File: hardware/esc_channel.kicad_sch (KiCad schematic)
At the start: 17 parts, among them Q32 AGM210MAP, Q33 AGM210MAP, Q34 AGM210MAP, U7 EFM8BB51F16I

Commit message: WIP hand-off: board sync progress, schematic readability edits (esc/pads/rx sheets), PDF; not yet verified
Co-Authored-By: Claude Opus 5.5 <noreply@anthropic.com>
Claude-Session: https://claude.ai/code/session_01RFaS5jnC9tnPam9GBgmGnG
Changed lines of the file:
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@@
 	(text_box "Power-up: the EFM8 runs from the cell before the FC's 3.3 V is up; its weak pull-up can put <= 60 uA on the FC DShot pad (0.72 V over the unpowered-FT limit, current-limited). Accepted on Matrix parity; V9 scopes it.\nUSB only: DShot idle-high back-feeds +BATT through the EFM8 I/O diode (about 1 mA per channel)."
 		(exclude_from_sim no)
-		(at 203.2 96.52 0)
+		(at 203.2 41.91 0)
 		(size 81.28 15.24)
 		(margins 0.9525 0.9525 0.9525 0.9525)

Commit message: Trim BOM to strictly needed parts, fill sourcing fields, fix library datasheets
Owner review 2026-10-11, schematic only (board not resynced).

Removed (17 parts): D1 TVS (clamps above every IC abs max), R2/R3/C5
INA186 input RC, U5 TPS22810 O4 switch with C16/C129/R9/R10/R87/D2
(VHD pad now on +5V_BST, as Matrix HD boards; HD_EN still holds the
analog VTX off via Q28, R11 kept), R67 selector (PA_VCC is +BATT),
TH1/R70 PA NTC and R84 (patched-ELRS only; GPIO37/GPIO4 no-connect),
C92 and C121 (beyond SX1281 / LP5912 datasheet decoupling).

Changed: D4 WS2812 VDD to +5V (3.5 V min); X3 TCXO pin 1 floating per
the YXC sheet; C122/C123/C134 4.7 uF 0402 -> 0201 GRM035R60J475ME15D.

Sourcing: LCSC numbers for 21 MPN lines (SKUBAAE010 has no listing);
every BOM part keeps MPN + Manufacturer for NextPCB.

Library: 16 unused lib symbols pruned; dead or HTML-only datasheet
links replaced with verified PDF URLs (RTC6705, SE5004L, FL2, X1,
EFM8BB51, BC857BM, FTC252012, HCS1206 shunt, Molex 53047).

Net-class patterns and contract entries for the removed nets dropped;
PINMAP ESP32 rows updated (GPIO36 is ADC1_CH0).

Validation: ERC 0 errors / 2 warnings (baseline); check_netlist 7 ok;
sch_integrate --check idempotent; check_conventions unchanged.

Co-Authored-By: Claude Opus 5.5 <noreply@anthropic.com>
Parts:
- R23, R24, R25: LCSC (none) -> C138165
- U7: LCSC (none) -> C3232998
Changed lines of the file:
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@@
 		(in_pos_files no)
 		(dnp no)
-		(property "Reference" "#PWR69"
+		(property "Reference" "#PWR60"
 			(at 109.22 153.67 0)
 			(hide yes)
@@
 			(project "OpenAIO-Whoop"
 				(path "/2c3a7206-1e66-4d43-a02f-491225e20dd6/0021bee0-9959-5c9e-86f0-21e49fa9ce8d"
-					(reference "#PWR69")
+					(reference "#PWR60")
 					(unit 1)
 				)
 				(path "/2c3a7206-1e66-4d43-a02f-491225e20dd6/6d139bfe-ad39-5d26-964c-e430887c2538"
-					(reference "#PWR89")
+					(reference "#PWR80")
 					(unit 1)
 				)
 				(path "/2c3a7206-1e66-4d43-a02f-491225e20dd6/a3c0517e-76c5-5fd7-8d0f-d7e948ad3995"
-					(reference "#PWR79")
+					(reference "#PWR70")
 					(unit 1)
 				)
 				(path "/2c3a7206-1e66-4d43-a02f-491225e20dd6/d67c44eb-67d1-5da8-b7a8-40b16f9433cd"
-					(reference "#PWR59")
+					(reference "#PWR50")
 					(unit 1)
 				)
@@
 			)
 		)
-		(property "LCSC" ""
+		(property "LCSC" "C3232998"
 			(at 76.2 60.96 0)
 			(hide yes)
@@
 		(in_pos_files no)
 		(dnp no)
-		(property "Reference" "#PWR72"
+		(property "Reference" "#PWR63"
 			(at 99.06 177.8 0)
 			(hide yes)
@@
 			(project "OpenAIO-Whoop"
 				(path "/2c3a7206-1e66-4d43-a02f-491225e20dd6/0021bee0-9959-5c9e-86f0-21e49fa9ce8d"
-					(reference "#PWR72")
+					(reference "#PWR63")
 					(unit 1)
 				)
 				(path "/2c3a7206-1e66-4d43-a02f-491225e20dd6/6d139bfe-ad39-5d26-964c-e430887c2538"
-					(reference "#PWR92")
+					(reference "#PWR83")
 					(unit 1)
 				)
 				(path "/2c3a7206-1e66-4d43-a02f-491225e20dd6/a3c0517e-76c5-5fd7-8d0f-d7e948ad3995"
-					(reference "#PWR82")
+					(reference "#PWR73")
 					(unit 1)
 				)
 				(path "/2c3a7206-1e66-4d43-a02f-491225e20dd6/d67c44eb-67d1-5da8-b7a8-40b16f9433cd"
-					(reference "#PWR62")
+					(reference "#PWR53")
 					(unit 1)
 				)
@@
 			)
 		)
-		(property "LCSC" ""
+		(property "LCSC" "C138165"
 			(at 156.21 35.56 0)
 			(hide yes)
@@
 		(in_pos_files no)
 		(dnp no)
-		(property "Reference" "#PWR73"
+		(property "Reference" "#PWR64"
 			(at 142.24 177.8 0)
 			(hide yes)
@@
 			(project "OpenAIO-Whoop"
 				(path "/2c3a7206-1e66-4d43-a02f-491225e20dd6/0021bee0-9959-5c9e-86f0-21e49fa9ce8d"
-					(reference "#PWR73")
+					(reference "#PWR64")
 					(unit 1)
 				)
 				(path "/2c3a7206-1e66-4d43-a02f-491225e20dd6/6d139bfe-ad39-5d26-964c-e430887c2538"
-					(reference "#PWR93")
+					(reference "#PWR84")
 					(unit 1)
 				)
 				(path "/2c3a7206-1e66-4d43-a02f-491225e20dd6/a3c0517e-76c5-5fd7-8d0f-d7e948ad3995"
-					(reference "#PWR83")
+					(reference "#PWR74")
 					(unit 1)
 				)
 				(path "/2c3a7206-1e66-4d43-a02f-491225e20dd6/d67c44eb-67d1-5da8-b7a8-40b16f9433cd"
-					(reference "#PWR63")
+					(reference "#PWR54")
 					(unit 1)
 				)
@@
 		(in_pos_files no)
 		(dnp no)
-		(property "Reference" "#PWR66"
+		(property "Reference" "#PWR57"
 			(at 76.2 87.63 0)
 			(hide yes)
@@
 			(project "OpenAIO-Whoop"
 				(path "/2c3a7206-1e66-4d43-a02f-491225e20dd6/0021bee0-9959-5c9e-86f0-21e49fa9ce8d"
-					(reference "#PWR66")
+					(reference "#PWR57")
 					(unit 1)
 				)
 				(path "/2c3a7206-1e66-4d43-a02f-491225e20dd6/6d139bfe-ad39-5d26-964c-e430887c2538"
-					(reference "#PWR86")
+					(reference "#PWR77")
 					(unit 1)
 				)
 				(path "/2c3a7206-1e66-4d43-a02f-491225e20dd6/a3c0517e-76c5-5fd7-8d0f-d7e948ad3995"
-					(reference "#PWR76")
+					(reference "#PWR67")
 					(unit 1)
 				)
 				(path "/2c3a7206-1e66-4d43-a02f-491225e20dd6/d67c44eb-67d1-5da8-b7a8-40b16f9433cd"
-					(reference "#PWR56")
+					(reference "#PWR47")
 					(unit 1)
 				)
@@
 			)
 		)
-		(property "LCSC" ""
+		(property "LCSC" "C138165"
 			(at 156.21 71.12 0)
 			(hide yes)
@@
 		(in_pos_files no)
 		(dnp no)
-		(property "Reference" "#PWR68"
+		(property "Reference" "#PWR59"
 			(at 66.04 153.67 0)
 			(hide yes)
@@
 			(project "OpenAIO-Whoop"
 				(path "/2c3a7206-1e66-4d43-a02f-491225e20dd6/0021bee0-9959-5c9e-86f0-21e49fa9ce8d"
-					(reference "#PWR68")
+					(reference "#PWR59")
 					(unit 1)
 				)
 				(path "/2c3a7206-1e66-4d43-a02f-491225e20dd6/6d139bfe-ad39-5d26-964c-e430887c2538"
-					(reference "#PWR88")
+					(reference "#PWR79")
 					(unit 1)
 				)
 				(path "/2c3a7206-1e66-4d43-a02f-491225e20dd6/a3c0517e-76c5-5fd7-8d0f-d7e948ad3995"
-					(reference "#PWR78")
+					(reference "#PWR69")
 					(unit 1)
 				)
 				(path "/2c3a7206-1e66-4d43-a02f-491225e20dd6/d67c44eb-67d1-5da8-b7a8-40b16f9433cd"
-					(reference "#PWR58")
+					(reference "#PWR49")
 					(unit 1)
 				)
@@
 			)
 		)
-		(property "LCSC" ""
+		(property "LCSC" "C138165"
 			(at 156.21 53.34 0)
 			(hide yes)
@@
 		(in_pos_files no)
 		(dnp no)
-		(property "Reference" "#PWR64"
+		(property "Reference" "#PWR55"
 			(at 76.2 31.75 0)
 			(hide yes)
@@
 			(project "OpenAIO-Whoop"
 				(path "/2c3a7206-1e66-4d43-a02f-491225e20dd6/0021bee0-9959-5c9e-86f0-21e49fa9ce8d"
-					(reference "#PWR64")
+					(reference "#PWR55")
 					(unit 1)
 				)
 				(path "/2c3a7206-1e66-4d43-a02f-491225e20dd6/6d139bfe-ad39-5d26-964c-e430887c2538"
-					(reference "#PWR84")
+					(reference "#PWR75")
 					(unit 1)
 				)
 				(path "/2c3a7206-1e66-4d43-a02f-491225e20dd6/a3c0517e-76c5-5fd7-8d0f-d7e948ad3995"
-					(reference "#PWR74")
+					(reference "#PWR65")
 					(unit 1)
 				)
 				(path "/2c3a7206-1e66-4d43-a02f-491225e20dd6/d67c44eb-67d1-5da8-b7a8-40b16f9433cd"
-					(reference "#PWR54")
+					(reference "#PWR45")
 					(unit 1)
 				)
@@
 		(in_pos_files no)
 		(dnp no)
-		(property "Reference" "#PWR65"
+		(property "Reference" "#PWR56"
 			(at 58.42 49.53 0)
 			(hide yes)
@@
 			(project "OpenAIO-Whoop"
 				(path "/2c3a7206-1e66-4d43-a02f-491225e20dd6/0021bee0-9959-5c9e-86f0-21e49fa9ce8d"
-					(reference "#PWR65")
+					(reference "#PWR56")
 					(unit 1)
 				)
 				(path "/2c3a7206-1e66-4d43-a02f-491225e20dd6/6d139bfe-ad39-5d26-964c-e430887c2538"
-					(reference "#PWR85")
+					(reference "#PWR76")
 					(unit 1)
 				)
 				(path "/2c3a7206-1e66-4d43-a02f-491225e20dd6/a3c0517e-76c5-5fd7-8d0f-d7e948ad3995"
-					(reference "#PWR75")
+					(reference "#PWR66")
 					(unit 1)
 				)
 				(path "/2c3a7206-1e66-4d43-a02f-491225e20dd6/d67c44eb-67d1-5da8-b7a8-40b16f9433cd"
-					(reference "#PWR55")
+					(reference "#PWR46")
 					(unit 1)
 				)
@@
 		(in_pos_files no)
 		(dnp no)
-		(property "Reference" "#PWR67"
+		(property "Reference" "#PWR58"
 			(at 22.86 143.51 0)
 			(hide yes)
@@
 			(project "OpenAIO-Whoop"
 				(path "/2c3a7206-1e66-4d43-a02f-491225e20dd6/0021bee0-9959-5c9e-86f0-21e49fa9ce8d"
-					(reference "#PWR67")
+					(reference "#PWR58")
 					(unit 1)
 				)
 				(path "/2c3a7206-1e66-4d43-a02f-491225e20dd6/6d139bfe-ad39-5d26-964c-e430887c2538"
-					(reference "#PWR87")
+					(reference "#PWR78")
 					(unit 1)
 				)
 				(path "/2c3a7206-1e66-4d43-a02f-491225e20dd6/a3c0517e-76c5-5fd7-8d0f-d7e948ad3995"
-					(reference "#PWR77")
+					(reference "#PWR68")
 					(unit 1)
 				)
 				(path "/2c3a7206-1e66-4d43-a02f-491225e20dd6/d67c44eb-67d1-5da8-b7a8-40b16f9433cd"
-					(reference "#PWR57")
+					(reference "#PWR48")
 					(unit 1)
 				)
@@
 		(in_pos_files no)
 		(dnp no)
-		(property "Reference" "#PWR71"
+		(property "Reference" "#PWR62"
 			(at 55.88 177.8 0)
 			(hide yes)
@@
 			(project "OpenAIO-Whoop"
 				(path "/2c3a7206-1e66-4d43-a02f-491225e20dd6/0021bee0-9959-5c9e-86f0-21e49fa9ce8d"
-					(reference "#PWR71")
+					(reference "#PWR62")
 					(unit 1)
 				)
 				(path "/2c3a7206-1e66-4d43-a02f-491225e20dd6/6d139bfe-ad39-5d26-964c-e430887c2538"
-					(reference "#PWR91")
+					(reference "#PWR82")
 					(unit 1)
 				)
 				(path "/2c3a7206-1e66-4d43-a02f-491225e20dd6/a3c0517e-76c5-5fd7-8d0f-d7e948ad3995"
-					(reference "#PWR81")
+					(reference "#PWR72")
 					(unit 1)
 				)
 				(path "/2c3a7206-1e66-4d43-a02f-491225e20dd6/d67c44eb-67d1-5da8-b7a8-40b16f9433cd"
-					(reference "#PWR61")
+					(reference "#PWR52")
 					(unit 1)
 				)
@@
 		(in_pos_files no)
 		(dnp no)
-		(property "Reference" "#PWR70"
+		(property "Reference" "#PWR61"
 			(at 152.4 153.67 0)
 			(hide yes)
@@
 			(project "OpenAIO-Whoop"
 				(path "/2c3a7206-1e66-4d43-a02f-491225e20dd6/0021bee0-9959-5c9e-86f0-21e49fa9ce8d"
-					(reference "#PWR70")
+					(reference "#PWR61")
 					(unit 1)
 				)
 				(path "/2c3a7206-1e66-4d43-a02f-491225e20dd6/6d139bfe-ad39-5d26-964c-e430887c2538"
-					(reference "#PWR90")
+					(reference "#PWR81")
 					(unit 1)
 				)
 				(path "/2c3a7206-1e66-4d43-a02f-491225e20dd6/a3c0517e-76c5-5fd7-8d0f-d7e948ad3995"
-					(reference "#PWR80")
+					(reference "#PWR71")
 					(unit 1)
 				)
 				(path "/2c3a7206-1e66-4d43-a02f-491225e20dd6/d67c44eb-67d1-5da8-b7a8-40b16f9433cd"
-					(reference "#PWR60")
-					(unit 1)
-				)
+					(reference "#PWR51")
+					(unit 1)
+				)

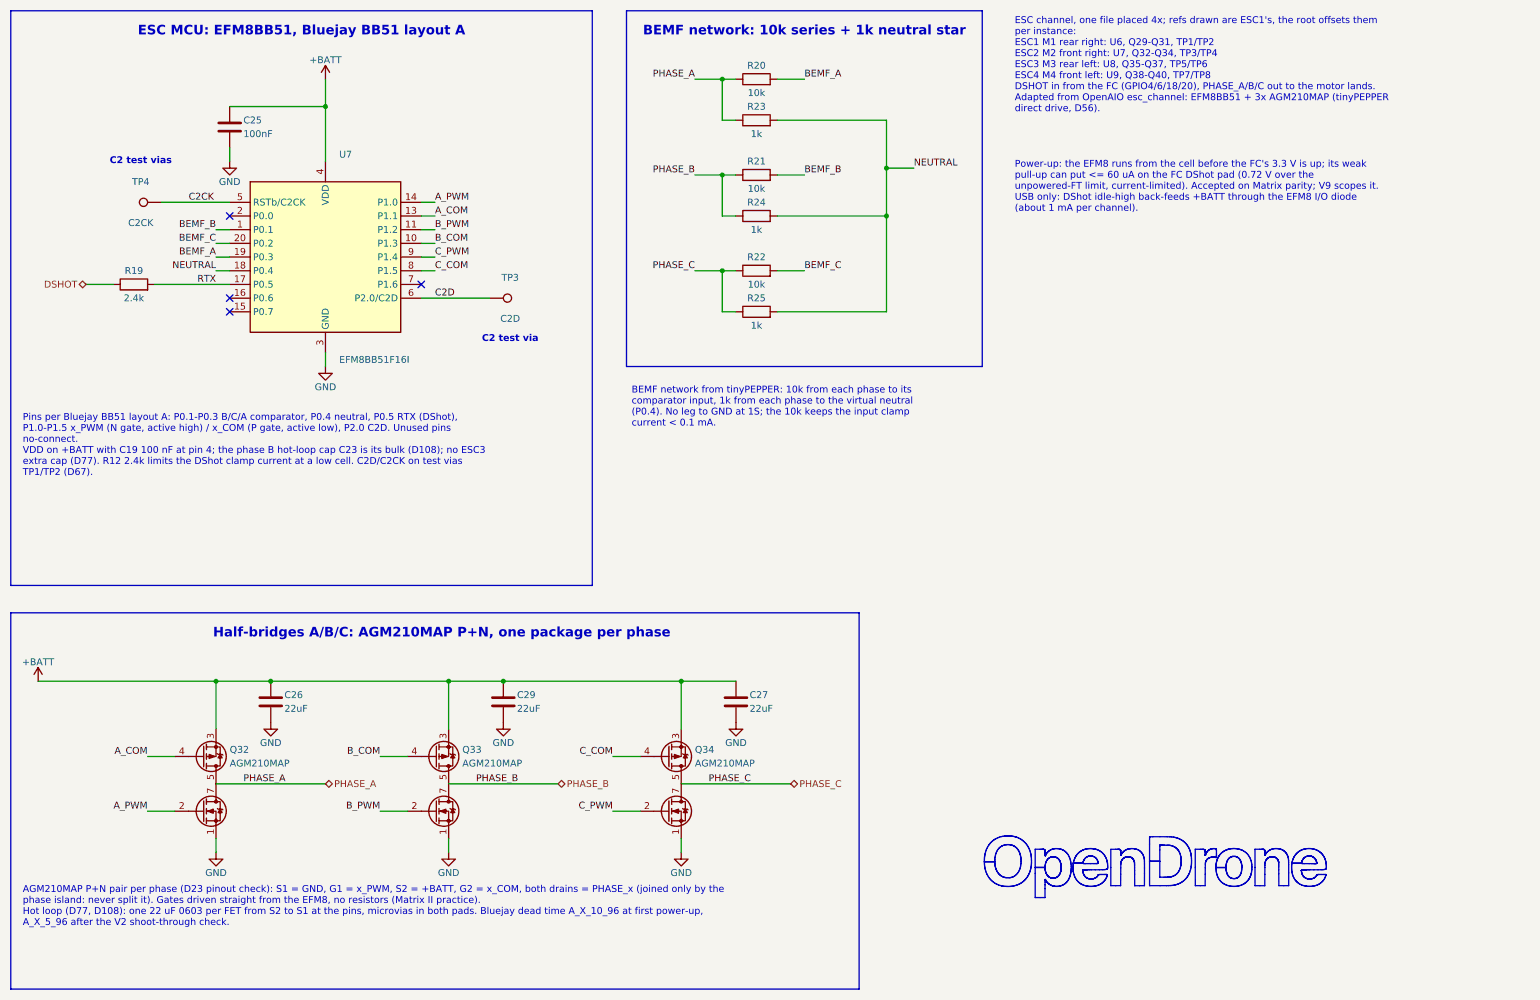
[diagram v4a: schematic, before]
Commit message: Footprint audit vs datasheets, 0201 lands to Murata minimum, schematic notes shortened
Footprints: 45 checked against their datasheets by group, no pin or
land errors. C/R/L_0201_..._L pad height 0.28 -> 0.30 (Murata GRM03
reflow table c >= 0.30); other lands already at least density per D109
and left unchanged. Land spec texts cleaned (sources, shared parts).

Schematic notes: 157 -> 152 items, 19.5k -> 9.7k characters, all
current (diode-OR, removed parts, RTC6705 filters, TX0/RX0).

check_footprint 107/107 lib specs PASS; ERC 0 errors / 2 warnings;
check_netlist 7 ok; sch_integrate --check clean. Board not synced.

Co-Authored-By: Claude Opus 5.5 <noreply@anthropic.com>
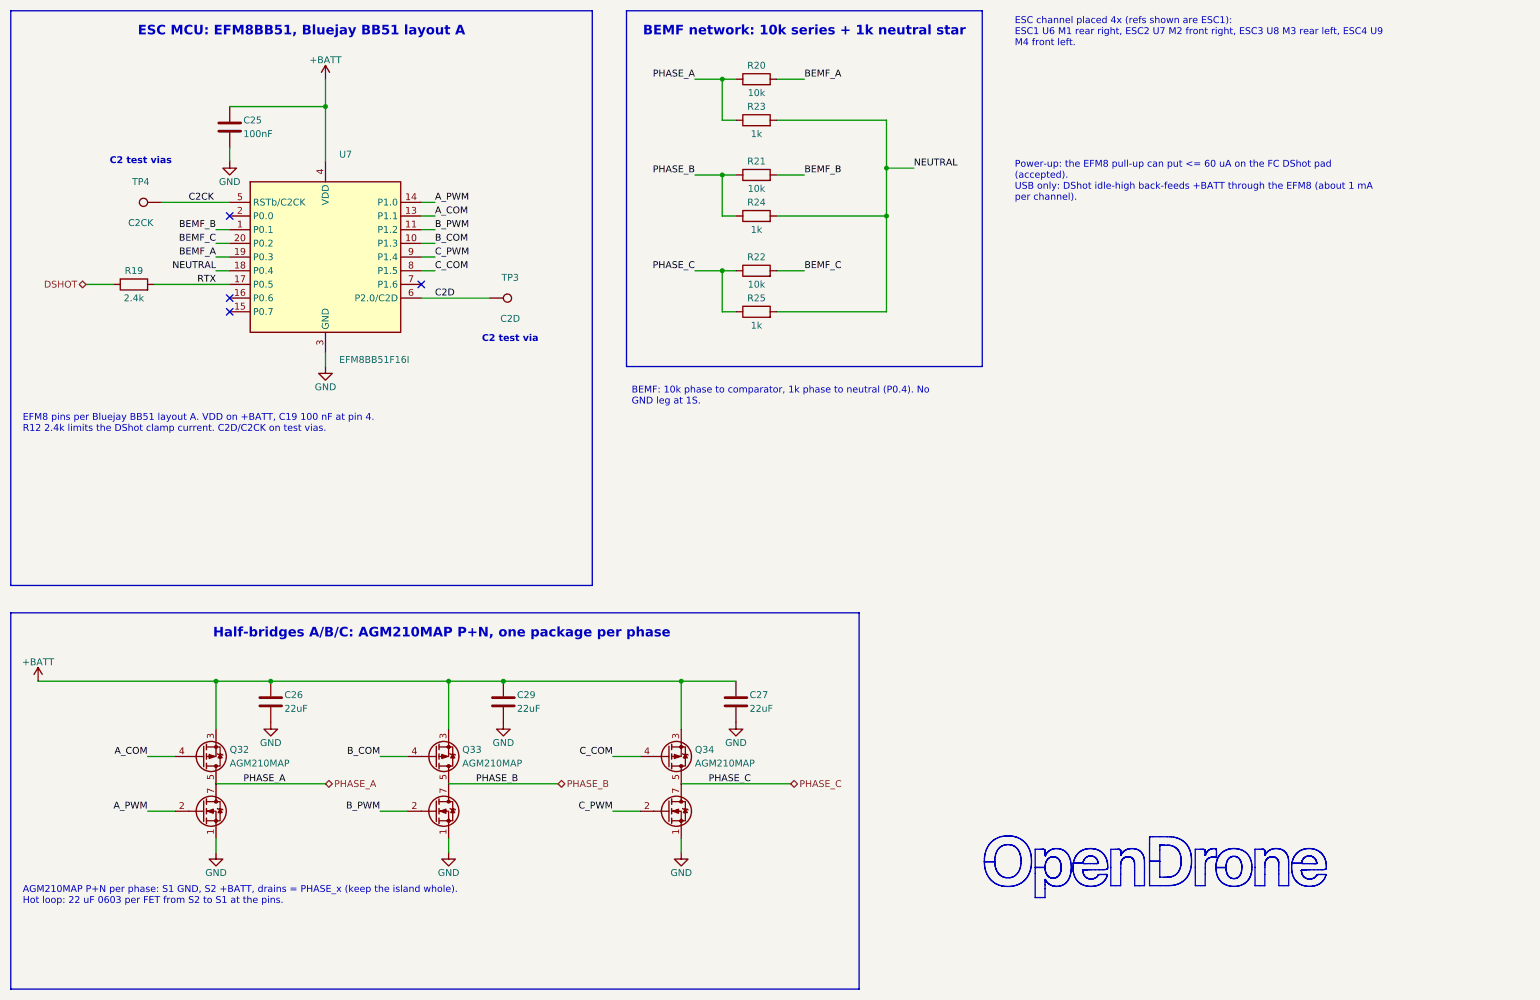
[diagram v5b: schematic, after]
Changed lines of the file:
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@@
 		)
 	)
-	(text_box "AGM210MAP P+N pair per phase (D23 pinout check): S1 = GND, G1 = x_PWM, S2 = +BATT, G2 = x_COM, both drains = PHASE_x (joined only by the phase island: never split it). Gates driven straight from the EFM8, no resistors (Matrix II practice).\nHot loop (D77, D108): one 22 uF 0603 per FET from S2 to S1 at the pins, microvias in both pads. Bluejay dead time A_X_10_96 at first power-up, A_X_5_96 after the V2 shoot-through check."
+	(text_box "AGM210MAP P+N per phase: S1 GND, S2 +BATT, drains = PHASE_x (keep the island whole).\nHot loop: 22 uF 0603 per FET from S2 to S1 at the pins."
 		(exclude_from_sim no)
 		(at 19.05 176.53 0)
@@
 		)
 	)
-	(text_box "ESC channel, one file placed 4x; refs drawn are ESC1's, the root offsets them per instance:\nESC1 M1 rear right: U6, Q29-Q31, TP1/TP2\nESC2 M2 front right: U7, Q32-Q34, TP3/TP4\nESC3 M3 rear left: U8, Q35-Q37, TP5/TP6\nESC4 M4 front left: U9, Q38-Q40, TP7/TP8\nDSHOT in from the FC (GPIO4/6/18/20), PHASE_A/B/C out to the motor lands. Adapted from OpenAIO esc_channel: EFM8BB51 + 3x AGM210MAP (tinyPEPPER direct drive, D56)."
+	(text_box "ESC channel placed 4x (refs shown are ESC1):\nESC1 U6 M1 rear right, ESC2 U7 M2 front right, ESC3 U8 M3 rear left, ESC4 U9 M4 front left."
 		(exclude_from_sim no)
 		(at 203.2 15.24 0)
@@
 		)
 	)
-	(text_box "Power-up: the EFM8 runs from the cell before the FC's 3.3 V is up; its weak pull-up can put <= 60 uA on the FC DShot pad (0.72 V over the unpowered-FT limit, current-limited). Accepted on Matrix parity; V9 scopes it.\nUSB only: DShot idle-high back-feeds +BATT through the EFM8 I/O diode (about 1 mA per channel)."
+	(text_box "Power-up: the EFM8 pull-up can put <= 60 uA on the FC DShot pad (accepted).\nUSB only: DShot idle-high back-feeds +BATT through the EFM8 (about 1 mA per channel)."
 		(exclude_from_sim no)
 		(at 203.2 41.91 0)
@@
 		)
 	)
-	(text_box "Pins per Bluejay BB51 layout A: P0.1-P0.3 B/C/A comparator, P0.4 neutral, P0.5 RTX (DShot), P1.0-P1.5 x_PWM (N gate, active high) / x_COM (P gate, active low), P2.0 C2D. Unused pins no-connect.\nVDD on +BATT with C19 100 nF at pin 4; the phase B hot-loop cap C23 is its bulk (D108); no ESC3 extra cap (D77). R12 2.4k limits the DShot clamp current at a low cell. C2D/C2CK on test vias TP1/TP2 (D67)."
+	(text_box "EFM8 pins per Bluejay BB51 layout A. VDD on +BATT, C19 100 nF at pin 4.\nR12 2.4k limits the DShot clamp current. C2D/C2CK on test vias."
 		(exclude_from_sim no)
 		(at 19.05 88.9 0)
@@
 		)
 	)
-	(text_box "BEMF network from tinyPEPPER: 10k from each phase to its comparator input, 1k from each phase to the virtual neutral (P0.4). No leg to GND at 1S; the 10k keeps the input clamp current < 0.1 mA."
+	(text_box "BEMF: 10k phase to comparator, 1k phase to neutral (P0.4). No GND leg at 1S."
 		(exclude_from_sim no)
 		(at 132.08 83.82 0)

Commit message: Larger solder pads and ESC programming pads, R1 shunt flipped (D120)
All hand-solder pads J20-J29/J33 on SolderPad_1.0x1.2mm; ESC C2 test
pads TP1-TP8 on TestPoint_Pad_D0.8mm; R1 rotated 270 without mirror
(owner edit, Kelvin pairs and INA186 polarity unchanged). ERC 0 errors;
check_netlist 7 ok.

Co-Authored-By: Claude Opus 5.5 <noreply@anthropic.com>
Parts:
- TP3, TP4: footprint lib:TestPoint_Pad_D0.30mm_MicroVia_L -> lib:TestPoint_Pad_D0.8mm
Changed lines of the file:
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@@
 			)
 		)
-		(property "Footprint" "lib:TestPoint_Pad_D0.30mm_MicroVia_L"
+		(property "Footprint" "lib:TestPoint_Pad_D0.8mm"
 			(at 106.68 68.58 0)
 			(hide yes)
@@
 			)
 		)
-		(property "Footprint" "lib:TestPoint_Pad_D0.30mm_MicroVia_L"
+		(property "Footprint" "lib:TestPoint_Pad_D0.8mm"
 			(at 45.72 50.8 0)
 			(hide yes)
